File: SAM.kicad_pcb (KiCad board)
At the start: 2 copper layers, 136.5 x 75.2 mm, 33 parts, among them J1 Bus_Apple_II_Card_Side, U1 DAC08, U2 L7805, U3 LM380N, U4 74LS273

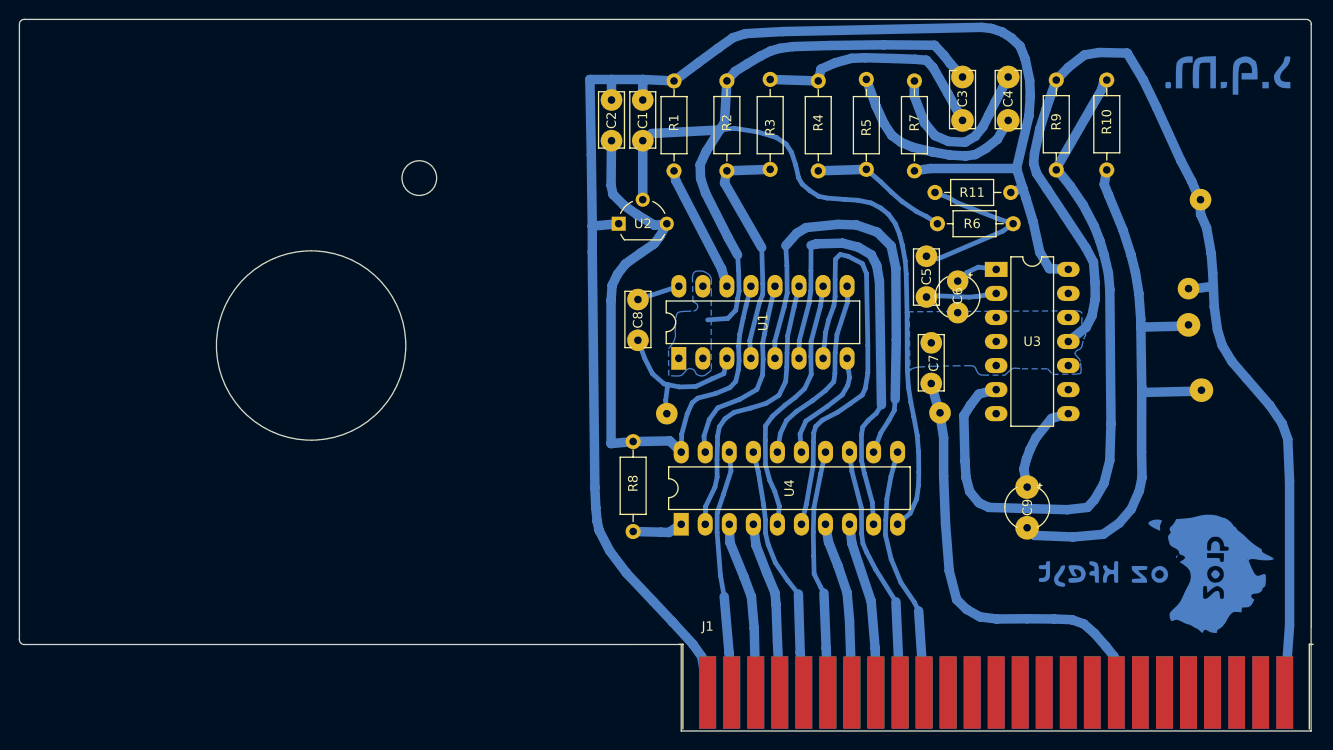
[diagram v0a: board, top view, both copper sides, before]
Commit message: chamfer traces so they look like manually done
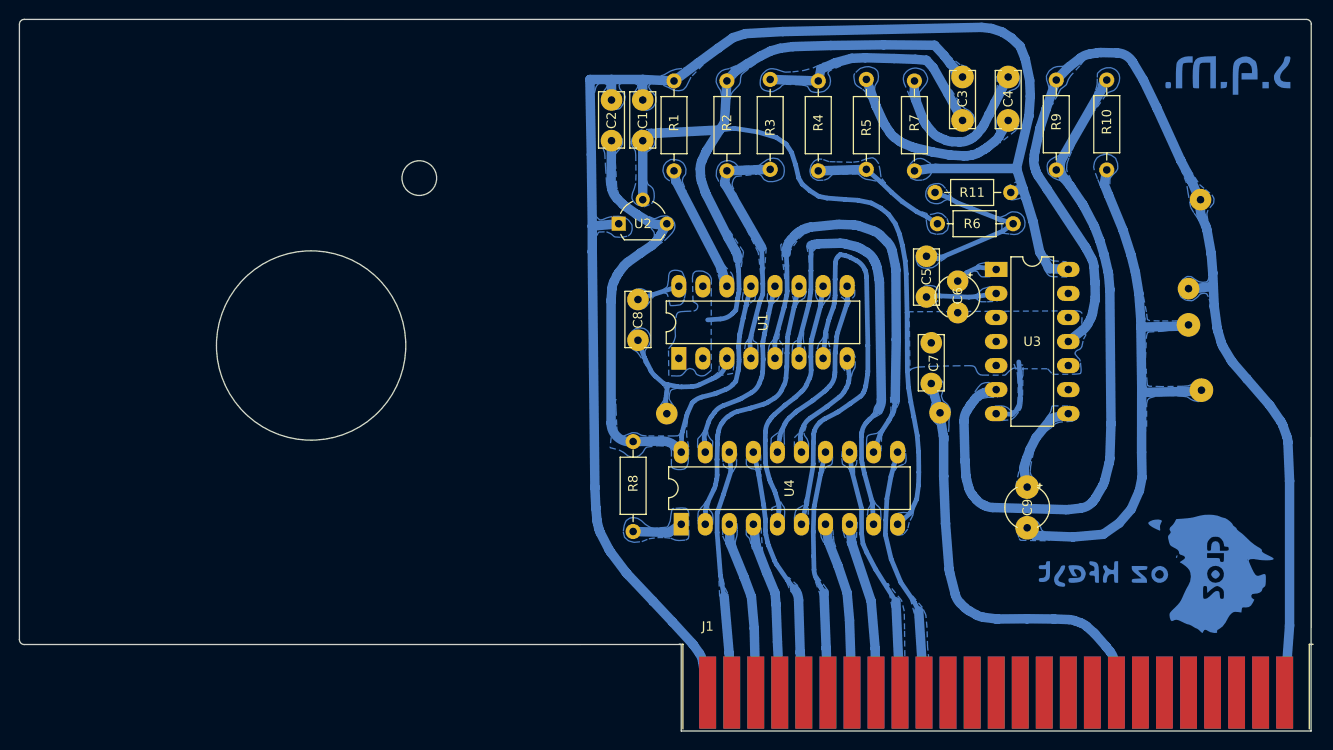
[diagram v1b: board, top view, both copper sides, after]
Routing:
- net GND: track 241.5 -> 248.6 mm
- net +5V: track 66.9 -> 65.5 mm
- net Net-(U3--): track 74.6 -> 74.0 mm
- added copper zone on B.Cu, net +12V
- added copper zone on B.Cu, net +5V
- added copper zone on B.Cu, net -12V
- added copper zone on B.Cu, net /B0
- added copper zone on B.Cu, net /B1
- added copper zone on B.Cu, net /B2
- added copper zone on B.Cu, net /B3
- added copper zone on B.Cu, net /B4
- added copper zone on B.Cu, net /B5
- added copper zone on B.Cu, net /B6
- added copper zone on B.Cu, net /B7
- added copper zone on B.Cu, net /D0
- added copper zone on B.Cu, net /D1
- added copper zone on B.Cu, net /D2
- added copper zone on B.Cu, net /D3
- added copper zone on B.Cu, net /D4
- added copper zone on B.Cu, net /D5
- added copper zone on B.Cu, net /D6
- added copper zone on B.Cu, net /D7
- added copper zone on B.Cu, net /~{DEVICE_SELECT}
- added copper zone on B.Cu, net Net-(C3-Pad1)
- added copper zone on B.Cu, net Net-(C4-Pad1)
- added copper zone on B.Cu, net Net-(C4-Pad2)
- added copper zone on B.Cu, net Net-(C5-Pad2)
- added copper zone on B.Cu, net Net-(C9-Pad1)
- added copper zone on B.Cu, net Net-(J2-Pin_2)
- added copper zone on B.Cu, net Net-(R4-Pad1)
- added copper zone on B.Cu, net Net-(U1-CMP)
- added copper zone on B.Cu, net Net-(U1-I-)
- added copper zone on B.Cu, net Net-(U1-R+)
- added copper zone on B.Cu, net Net-(U3-+)
- added copper zone on B.Cu, net Net-(U3--)
- added copper zone on B.Cu, net Net-(U3-BYPASS)
- added copper zone on B.Cu, net Net-(U4-~{Mr})
